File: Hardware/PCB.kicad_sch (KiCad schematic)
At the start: 13 parts, among them J1 Conn_01x05, SW1 SW_MEC_5E, U1 ME54BS01_V1.0, U2 MCP1700x-330xxTO

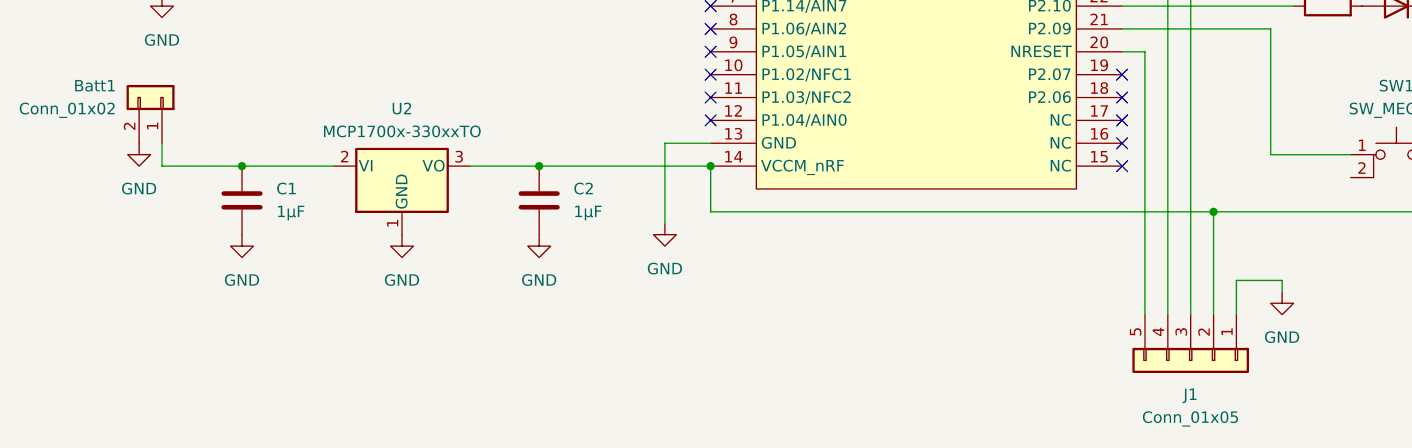
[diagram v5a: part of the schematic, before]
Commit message: PCB: Add another PIN to the header so power can be provided via J-Link.
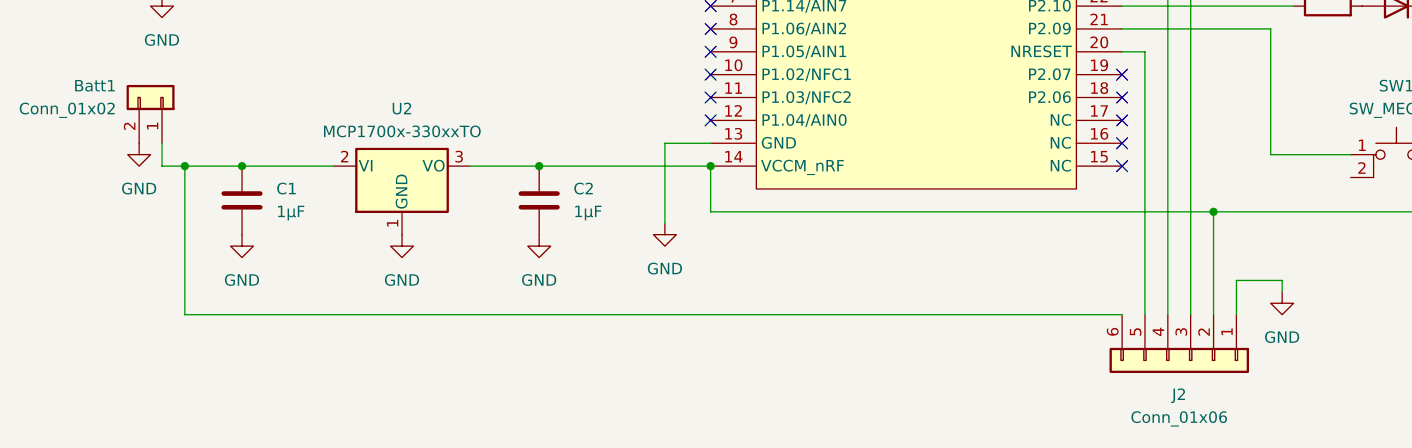
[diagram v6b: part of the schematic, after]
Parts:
- removed J1: Conn_01x05, Connector_PinHeader_2.54mm:PinHeader_1x05_P2.54mm_Vertical, symbol Connector_Generic:Conn_01x05
- added J2: Conn_01x06, Connector_PinHeader_2.54mm:PinHeader_1x06_P2.54mm_Vertical, symbol Connector_Generic:Conn_01x06
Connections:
- net GND: now also J2.1 (Pin_1)
- net at Batt1.1 (Pin_1), C1.1, U2.2 (VI): now also J2.6 (Pin_6)
- net at C2.1, SW1.4 (A), U1.14 (VCCM_nRF)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: now also J2.2 (Pin_2)
- net at U1.20 (NRESET): now also J2.5 (Pin_5)
- net at U1.25 (SWDIO): now also J2.4 (Pin_4)
- net at U1.26 (SWDCLK): now also J2.3 (Pin_3)
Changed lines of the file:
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@@
+	)
+	(junction
+		(at 96.52 60.96)
+		(diameter 0)
+		(color 0 0 0 0)
 	)
 	(junction
@@
 	(wire
 		(pts
-			(xy 93.98 60.96) (xy 102.87 60.96)
+			(xy 93.98 60.96) (xy 96.52 60.96)
 		)
 		(stroke
@@
 	(wire
 		(pts
+			(xy 200.66 77.47) (xy 96.52 77.47)
+		)
+		(stroke
+			(width 0)
+			(type default)
+		)
+	)
+	(wire
+		(pts
 			(xy 210.82 66.04) (xy 210.82 77.47)
 		)
@@
 	(wire
 		(pts
+			(xy 96.52 60.96) (xy 102.87 60.96)
+		)
+		(stroke
+			(width 0)
+			(type default)
+		)
+	)
+	(wire
+		(pts
 			(xy 218.44 73.66) (xy 218.44 74.93)
 		)
@@
 		(pts
 			(xy 96.52 30.48) (xy 115.57 30.48)
+		)
+		(stroke
+			(width 0)
+			(type default)
+		)
+	)
+	(wire
+		(pts
+			(xy 96.52 77.47) (xy 96.52 60.96)
 		)
 		(stroke
@@
 	)
 	(symbol
-		(lib_id "Connector_Generic:Conn_01x05")
+		(lib_id "Connector_Generic:Conn_01x06")
 		(at 208.28 82.55 270)
 		(unit 1)
@@
 		(dnp no)
 		(fields_autoplaced yes)
-		(property "Reference" "J1"
-			(at 208.28 86.36 90)
-			(effects
-				(font
-					(size 1.27 1.27)
-				)
-			)
-		)
-		(property "Value" "Conn_01x05"
-			(at 208.28 88.9 90)
-			(effects
-				(font
-					(size 1.27 1.27)
-				)
-			)
-		)
-		(property "Footprint" "Connector_PinHeader_2.54mm:PinHeader_1x05_P2.54mm_Vertical"
+		(property "Reference" "J2"
+			(at 207.01 86.36 90)
+			(effects
+				(font
+					(size 1.27 1.27)
+				)
+			)
+		)
+		(property "Value" "Conn_01x06"
+			(at 207.01 88.9 90)
+			(effects
+				(font
+					(size 1.27 1.27)
+				)
+			)
+		)
+		(property "Footprint" "Connector_PinHeader_2.54mm:PinHeader_1x06_P2.54mm_Vertical"
 			(at 208.28 82.55 0)
 			(effects
@@
 			)
 		)
-		(property "Description" "Generic connector, single row, 01x05, script generated (kicad-library-utils/schlib/autogen/connector/)"
+		(property "Description" "Generic connector, single row, 01x06, script generated (kicad-library-utils/schlib/autogen/connector/)"
 			(at 208.28 82.55 0)
 			(effects
@@
 			)
 		)
+		(pin "4"
+		)
+		(pin "6"
+		)
+		(pin "2"
+		)
+		(pin "1"
+		)
+		(pin "3"
+		)
 		(pin "5"
 		)
-		(pin "3"
-		)
-		(pin "1"
-		)
-		(pin "2"
-		)
-		(pin "4"
-		)
 		(instances
 			(project ""
 				(path "/9240e15d-484a-49b3-8f80-37d1a010783e"
-					(reference "J1")
-					(unit 1)
-				)
+					(reference "J2")
+					(unit 1)
+				)

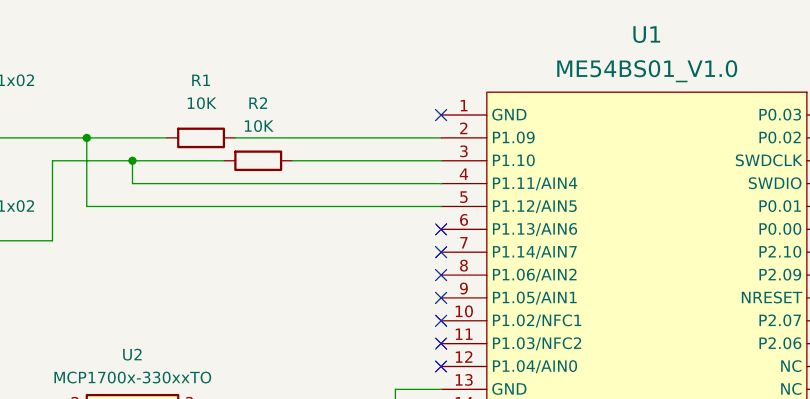
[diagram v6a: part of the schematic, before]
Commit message: Move decoupling capacitors closer to LDO. Ground module PIN 1.
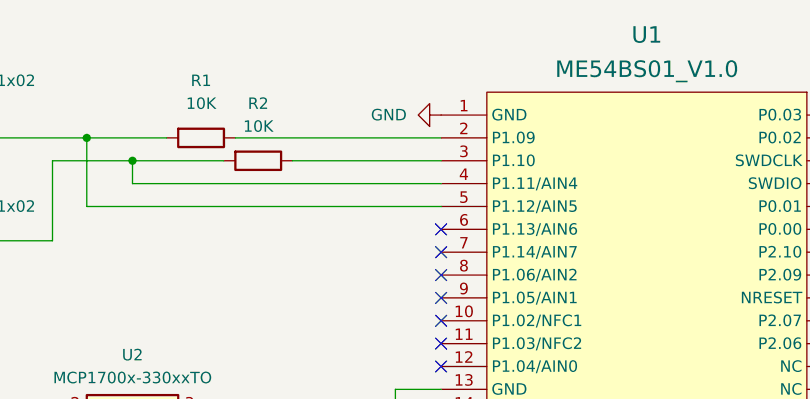
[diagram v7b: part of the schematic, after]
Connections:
- net GND: now also U1.1 (GND)
- no-connect marks 17 -> 16
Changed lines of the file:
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@@
 		(at 200.66 55.88)
 	)
-	(no_connect
-		(at 154.94 27.94)
-	)
 	(wire
 		(pts
@@
 		)
 	)
+	(symbol
+		(lib_name "GND_5")
+		(lib_id "power:GND")
+		(at 154.94 27.94 270)
+		(unit 1)
+		(exclude_from_sim no)
+		(in_bom yes)
+		(on_board yes)
+		(dnp no)
+		(fields_autoplaced yes)
+		(property "Reference" "#PWR010"
+			(at 148.59 27.94 0)
+			(effects
+				(font
+					(size 1.27 1.27)
+				)
+				(hide yes)
+			)
+		)
+		(property "Value" "GND"
+			(at 151.13 27.9399 90)
+			(effects
+				(font
+					(size 1.27 1.27)
+				)
+				(justify right)
+			)
+		)
+		(property "Footprint" ""
+			(at 154.94 27.94 0)
+			(effects
+				(font
+					(size 1.27 1.27)
+				)
+				(hide yes)
+			)
+		)
+		(property "Datasheet" ""
+			(at 154.94 27.94 0)
+			(effects
+				(font
+					(size 1.27 1.27)
+				)
+				(hide yes)
+			)
+		)
+		(property "Description" "Power symbol creates a global label with name \"GND\" , ground"
+			(at 154.94 27.94 0)
+			(effects
+				(font
+					(size 1.27 1.27)
+				)
+				(hide yes)
+			)
+		)
+		(pin "1"
+		)
+		(instances
+			(project ""
+				(path "/9240e15d-484a-49b3-8f80-37d1a010783e"
+					(reference "#PWR010")
+					(unit 1)
+				)
+			)
+		)
+	)

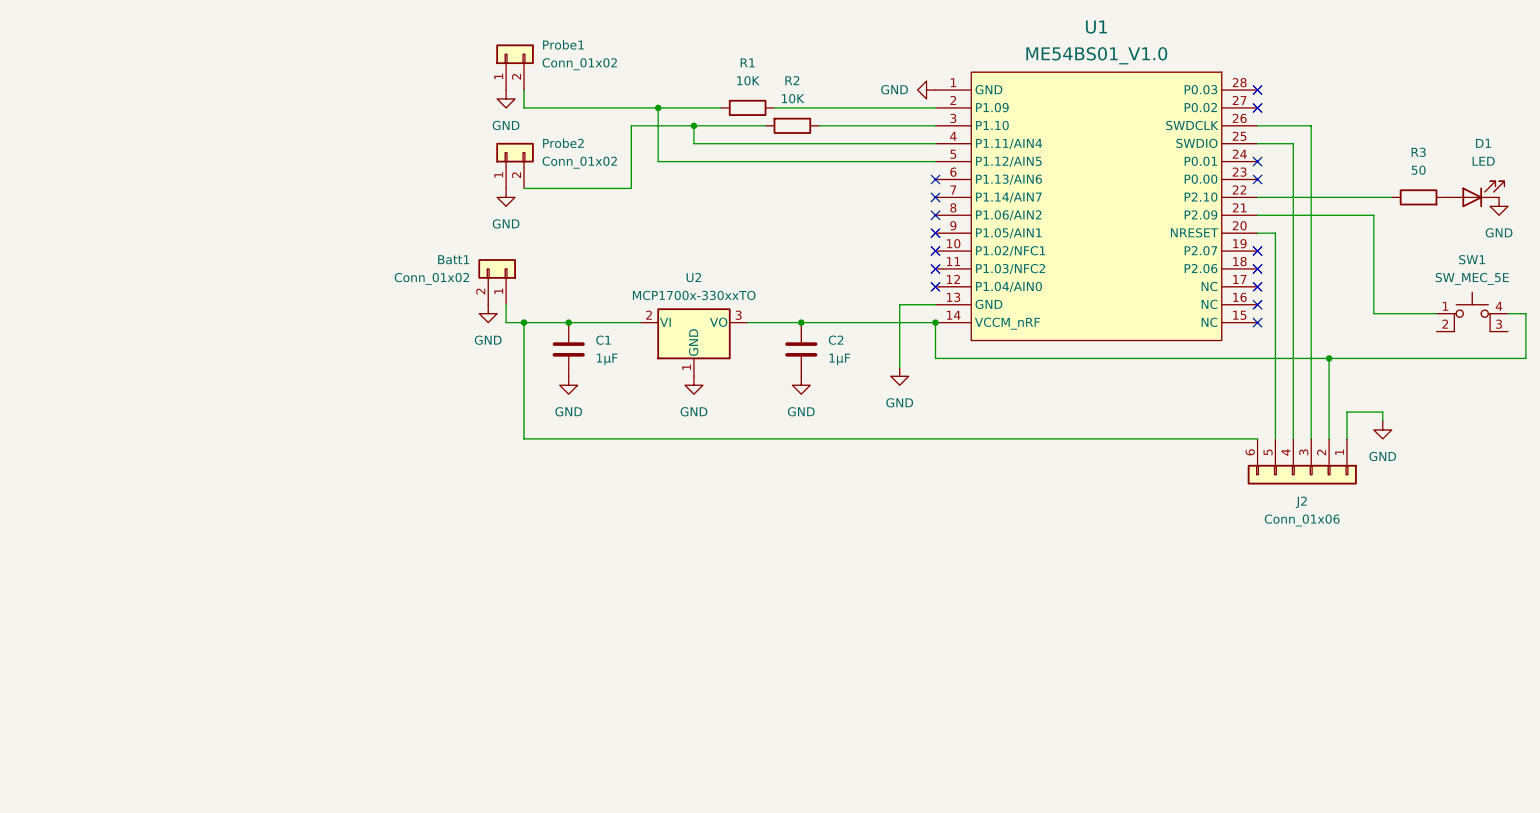
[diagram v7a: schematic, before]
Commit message: Update PCB with fix for LDO and tracing improvements.
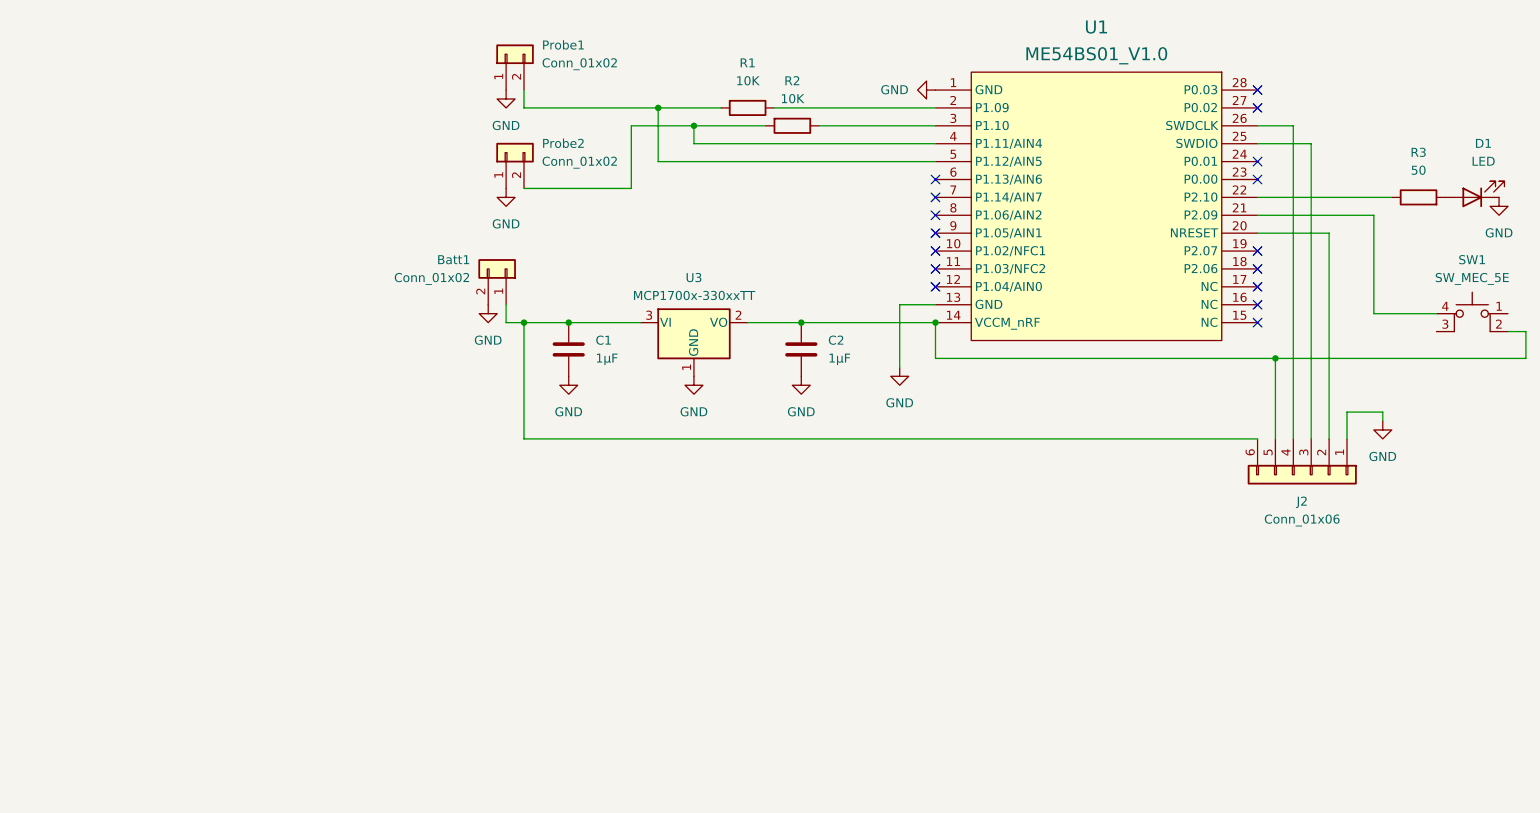
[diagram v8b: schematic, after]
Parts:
- removed U2: MCP1700x-330xxTO, Package_TO_SOT_SMD:SOT-23-3, symbol Regulator_Linear:MCP1700x-330xxTO
- added U3: MCP1700x-330xxTT, Package_TO_SOT_SMD:SOT-23, symbol Regulator_Linear:MCP1700x-330xxTT
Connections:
- net GND: now also U3.1 (GND)
- net at Batt1.1 (Pin_1), C1.1, J2.6 (Pin_6): now also U3.3 (VI)
- net at SW1.1: no longer U1.21 (P2.09)
- net at SW1.2: now also C2.1, J2.5 (Pin_5), U1.14 (VCCM_nRF), U3.2 (VO)
- net at U1.20 (NRESET): now also J2.2 (Pin_2); no longer J2.5 (Pin_5)
- net at U1.25 (SWDIO): now also J2.3 (Pin_3); no longer J2.4 (Pin_4)
- net at U1.26 (SWDCLK): now also J2.4 (Pin_4); no longer J2.3 (Pin_3)
- new net: SW1.4 (A), U1.21 (P2.09)
